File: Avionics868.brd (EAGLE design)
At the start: 86.4 x 22.9 mm, 69 parts, among them SW1 B3U-1000P-2P-SMD, U1 ATSAMD21G18_QFN, U2 SPX3819M5-L-3-0, U3 MCP73831T-2ACI/OT, U4 MPU-9250, U5 SIM868, U6 BMP280, X1 JSTPH, X2 32.768, X3 ZX62-B-5PA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

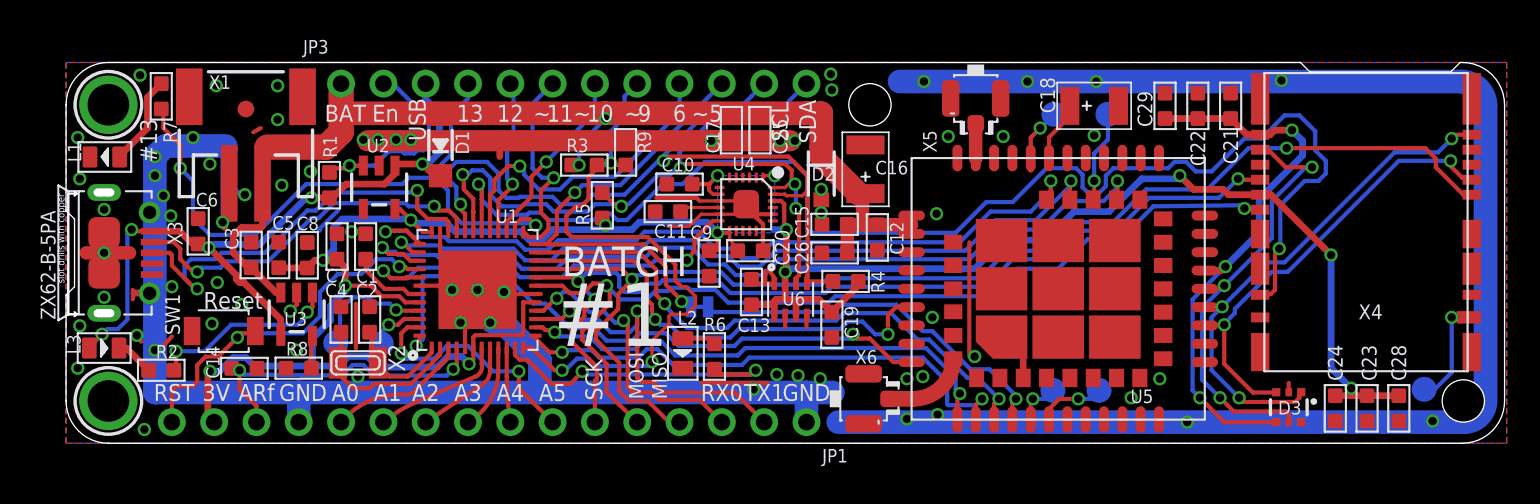
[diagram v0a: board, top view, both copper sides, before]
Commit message: Moved things around to improve capacitor placement
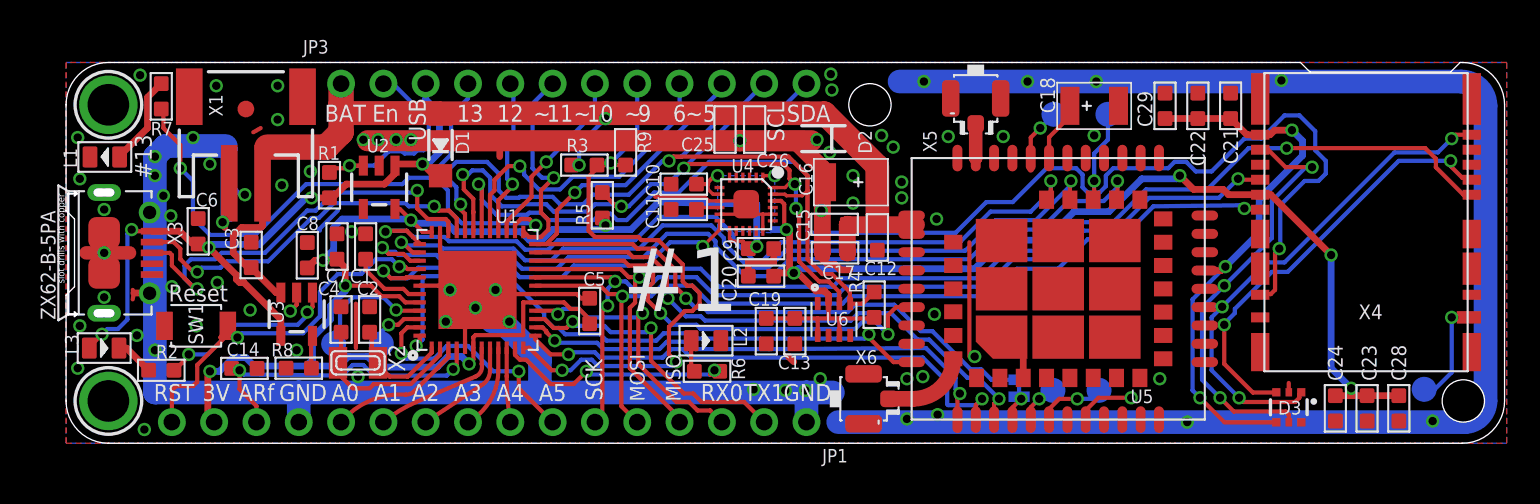
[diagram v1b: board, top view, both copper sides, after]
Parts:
- moved JP2 19.8 mm to (57.2, 3.30), turned to 270 degrees
- moved C5 19.0 mm to (31.4, 7.94)
- moved C17 9.64 mm to (46.2, 11.4), turned to 270 degrees
- moved C26 8.82 mm to (41.3, 18.8), turned to 180 degrees
- moved C19 3.96 mm to (42.0, 6.73)
- moved C13 3.51 mm to (43.8, 6.73), turned to 180 degrees
- moved C9 3.24 mm to (41.7, 11.7), turned to 270 degrees
- moved U6 2.87 mm to (46.1, 7.43)
- moved R4 2.21 mm to (48.5, 8.32), turned to 0 degrees
- moved D2 2.10 mm to (45.5, 18.3), turned to 180 degrees
- moved C25 2.10 mm to (39.6, 18.8)
- moved SW1 1.68 mm to (7.81, 7.05)
- moved C20 1.65 mm to (41.7, 10.0), turned to 90 degrees
- moved L2 1.59 mm to (38.4, 6.16), turned to 0 degrees
- moved C16 1.17 mm to (47.1, 15.7), turned to 180 degrees
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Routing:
- net D5/CTS2: track 27.0 -> 48.9 mm
- net N$6: track 22.6 -> 1.46 mm
- net GND: track 251.6 -> 262.6 mm, vias 70 -> 75
- net +3V: track 148.3 -> 157.6 mm
- net D8/GLED: track 18.7 -> 15.0 mm
- net MOSI: track 57.9 -> 55.1 mm
- net D1/TX0: track 20.6 -> 18.0 mm
- net MISO: track 74.4 -> 72.2 mm
- net SCL: track 47.8 -> 50.0 mm
- net SCK: track 58.3 -> 56.4 mm
- net SDA: track 46.9 -> 48.7 mm
- net N$23: track 3.16 -> 1.43 mm
- net VBAT: track 71.5 -> 73.0 mm
- net TX5/GPS_RX: track 47.5 -> 48.5 mm
- net RX5/GPS_TX: track 46.6 -> 47.5 mm
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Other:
- board text removed: "BATCH"

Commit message: Added some more connections to improve ground covg
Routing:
- net GND: vias 75 -> 98

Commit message: Switched Tantanum AVX-B caps with Ceramic C1206
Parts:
- C16, C18: device Seeed-Capacitor-2016:AVX-B -> Seeed-Capacitor-2016:C1206
- moved C16 0.27 mm to (46.9, 15.5)
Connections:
- net GND: now also C16.2, C18.2; no longer C16.-, C18.-
- net N$29: now also C18.1; no longer C18.+
- net VBAT: now also C16.1; no longer C16.+
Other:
- board text added: "GPS"
- board text added: "GSM"
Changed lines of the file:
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@@
 <layer number="25" name="tNames" color="7" fill="1" visible="yes" active="yes"/>
 <layer number="26" name="bNames" color="7" fill="1" visible="yes" active="yes"/>
-<layer number="27" name="tValues" color="7" fill="1" visible="yes" active="yes"/>
-<layer number="28" name="bValues" color="7" fill="1" visible="yes" active="yes"/>
+<layer number="27" name="tValues" color="7" fill="1" visible="no" active="yes"/>
+<layer number="28" name="bValues" color="7" fill="1" visible="no" active="yes"/>
 <layer number="29" name="tStop" color="7" fill="3" visible="yes" active="yes"/>
 <layer number="30" name="bStop" color="7" fill="6" visible="yes" active="yes"/>
@@
 <wire x1="74.676" y1="22.2885" x2="83.1215" y2="22.2885" width="0" layer="20"/>
 <wire x1="83.1215" y1="22.2885" x2="83.693" y2="22.86" width="0" layer="20"/>
+<text x="51.8795" y="20.7645" size="1.016" layer="21" ratio="12" rot="R270" align="center">GSM</text>
+<text x="48.006" y="5.2705" size="1.016" layer="21" ratio="12" rot="R180" align="center">GPS</text>
 </plain>
 <attributes>
@@
 <attribute name="VALUE" x="40.2971" y="12.7635" size="0.8128" layer="27" font="vector" ratio="18"/>
 </element>
-<element name="C16" library="Seeed-Capacitor-2016" package="AVX-B" value="100uf" x="47.117" y="15.6718" smashed="yes" rot="R180">
-<attribute name="MPN" value="TAJB107M010#NJ" x="47.117" y="26.3398" size="1.778" layer="27" rot="R180" display="off"/>
-<attribute name="NAME" x="44.0055" y="16.8402" size="0.8128" layer="25" ratio="18" rot="R270"/>
-<attribute name="VALUE" x="47.879" y="14.4018" size="0.8128" layer="27" ratio="18" rot="R90"/>
-<attribute name="NAME" x="47.6885" y="15.4178" size="0.4064" layer="33" ratio="18" rot="R180"/>
+<element name="C16" library="Seeed-Capacitor-2016" package="C1206" value="100uf" x="46.9265" y="15.4813" smashed="yes" rot="R180">
+<attribute name="MPN" value="GRM31CR60J107ME39L" x="46.9265" y="26.1493" size="1.778" layer="27" rot="R180" display="off"/>
+<attribute name="NAME" x="43.561" y="16.4592" size="0.8128" layer="25" ratio="18" rot="R270"/>
+<attribute name="VALUE" x="47.6885" y="14.2113" size="0.8128" layer="27" ratio="18" rot="R90"/>
+<attribute name="NAME" x="47.498" y="15.2273" size="0.4064" layer="33" ratio="18" rot="R180"/>
 </element>
 <element name="C17" library="Seeed-Capacitor-2016" package="C0603" value="10uf" x="46.1645" y="11.43" smashed="yes" rot="R270">
@@
 </element>
 <element name="X6" library="Seeed-Connector -2016" package="U-FL3P-SMD-2.6X2.6X1.0MM" value="U-FL" x="47.879" y="2.667" smashed="yes" rot="R180">
-<attribute name="NAME" x="48.7045" y="5.588" size="0.8128" layer="25" ratio="18" rot="R180"/>
+<attribute name="NAME" x="45.593" y="5.2705" size="0.8128" layer="25" ratio="18" rot="R270"/>
 </element>
 <element name="X5" library="Seeed-Connector -2016" package="U-FL3P-SMD-2.6X2.6X1.0MM" value="U-FL" x="54.61" y="20.701" smashed="yes" rot="R90">
-<attribute name="NAME" x="52.2605" y="17.4625" size="0.8128" layer="25" ratio="18" rot="R90"/>
+<attribute name="NAME" x="57.531" y="19.685" size="0.8128" layer="25" ratio="18" rot="R90"/>
 </element>
 <element name="TP4" library="microbuilder" package="TESTPOINT_ROUND_1.5MM" value="" x="62.5475" y="19.7485" smashed="yes" rot="MR0">
@@
 <attribute name="VALUE" x="78.0415" y="17.2215" size="0.889" layer="27" font="vector" ratio="18" rot="R180" align="center"/>
 </element>
-<element name="C18" library="Seeed-Capacitor-2016" package="AVX-B" value="100uf" x="61.722" y="20.2565" smashed="yes">
-<attribute name="MPN" value="TAJB107M010#NJ" x="61.722" y="20.2565" size="1.778" layer="27" display="off"/>
-<attribute name="NAME" x="59.3725" y="19.812" size="0.889" layer="25" ratio="11" rot="R90"/>
+<element name="C18" library="Seeed-Capacitor-2016" package="C1206" value="100uf" x="61.722" y="20.2565" smashed="yes">
+<attribute name="MPN" value="GRM31CR60J107ME39L" x="61.722" y="20.2565" size="1.778" layer="27" display="off"/>
+<attribute name="NAME" x="59.182" y="19.177" size="0.889" layer="25" ratio="11" rot="R90"/>
 <attribute name="VALUE" x="59.817" y="18.0975" size="0.635" layer="27" ratio="10"/>
 <attribute name="NAME" x="61.087" y="20.2565" size="0.4064" layer="33" ratio="10"/>
@@
 <wire x1="28.448" y1="5.0165" x2="28.448" y2="3.048" width="1.4224" layer="16"/>
 <wire x1="17.399" y1="5.715" x2="17.399" y2="8.382" width="0.254" layer="1"/>
-<contactref element="C18" pad="-"/>
+<contactref element="C18" pad="2"/>
 <contactref element="R9" pad="2"/>
 <via x="25.781" y="9.2075" extent="1-16" drill="0.5"/>
@@
 <contactref element="X5" pad="GND1"/>
 <contactref element="X5" pad="GND2"/>
-<contactref element="C16" pad="-"/>
+<contactref element="C16" pad="2"/>
 <contactref element="C17" pad="2"/>
 <contactref element="D2" pad="A"/>
@@
 <wire x1="30.7975" y1="17.907" x2="32.385" y2="19.4945" width="0.254" layer="16"/>
 <via x="32.385" y="19.4945" extent="1-16" drill="0.5"/>
-<contactref element="C16" pad="+"/>
+<contactref element="C16" pad="1"/>
 <contactref element="C17" pad="1"/>
 <contactref element="C12" pad="1"/>
@@
 <wire x1="22.479" y1="19.757" x2="22.479" y2="20.32" width="0.4064" layer="1"/>
 <wire x1="22.479" y1="20.32" x2="16.51" y2="20.32" width="0.4064" layer="1"/>
-<wire x1="48.7045" y1="16.637" x2="48.5775" y2="15.6718" width="0" layer="19" extent="1-1"/>
+<wire x1="48.7045" y1="16.637" x2="48.5775" y2="15.4813" width="0" layer="19" extent="1-1"/>
 <wire x1="48.7045" y1="13.1191" x2="48.7045" y2="13.335" width="0" layer="19" extent="1-1"/>
 <wire x1="50.763" y1="13.671" x2="51.054" y2="13.1191" width="0" layer="19" extent="1-1"/>
@@
 <signal name="N$29">
 <contactref element="U5" pad="28_"/>
-<contactref element="C18" pad="+"/>
+<contactref element="C18" pad="1"/>
 <wire x1="59.013" y1="17.121" x2="59.013" y2="18.373" width="0.254" layer="1"/>
 <wire x1="59.013" y1="18.373" x2="60.2615" y2="19.6215" width="0.254" layer="1"/>
-<wire x1="60.2615" y1="19.6215" x2="60.2615" y2="20.2565" width="0.254" layer="1"/>
+<wire x1="60.2615" y1="19.6215" x2="60.071" y2="20.2565" width="0.254" layer="1"/>
 </signal>
 <signal name="GPS_ANT">

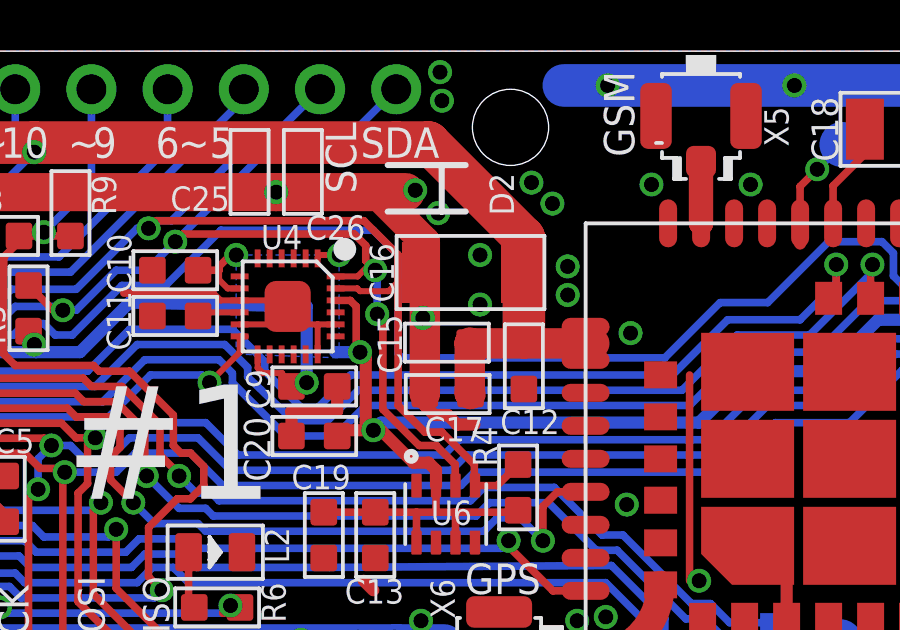
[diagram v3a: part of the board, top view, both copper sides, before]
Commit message: fixed a short circuit introduced when changing the 100uF caps to ceramic
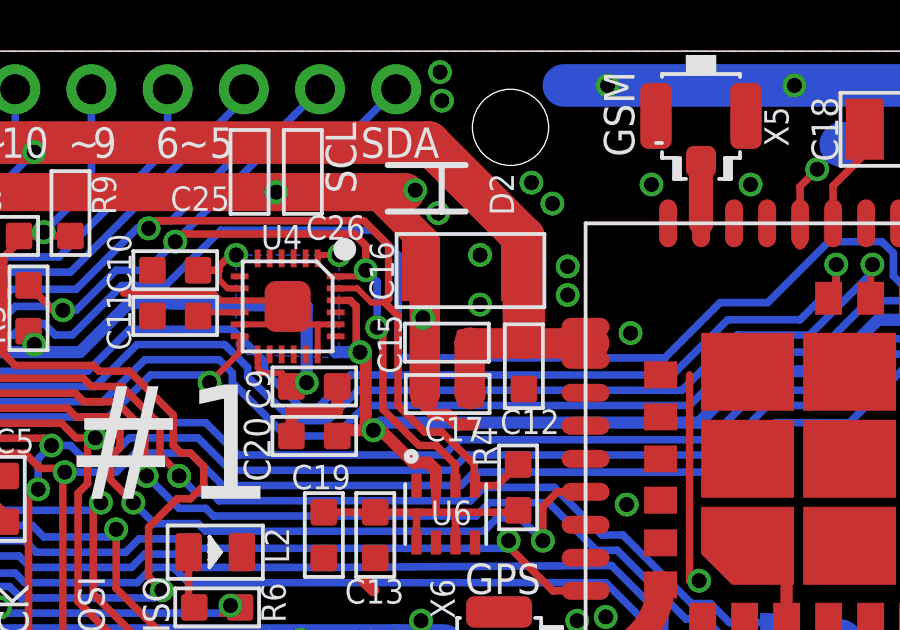
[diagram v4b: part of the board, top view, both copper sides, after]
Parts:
- moved C16 0.06 mm to (46.9, 15.5)
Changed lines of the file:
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@@
 <attribute name="VALUE" x="40.2971" y="12.7635" size="0.8128" layer="27" font="vector" ratio="18"/>
 </element>
-<element name="C16" library="Seeed-Capacitor-2016" package="C1206" value="100uf" x="46.9265" y="15.4813" smashed="yes" rot="R180">
-<attribute name="MPN" value="GRM31CR60J107ME39L" x="46.9265" y="26.1493" size="1.778" layer="27" rot="R180" display="off"/>
-<attribute name="NAME" x="43.561" y="16.4592" size="0.8128" layer="25" ratio="18" rot="R270"/>
-<attribute name="VALUE" x="47.6885" y="14.2113" size="0.8128" layer="27" ratio="18" rot="R90"/>
-<attribute name="NAME" x="47.498" y="15.2273" size="0.4064" layer="33" ratio="18" rot="R180"/>
+<element name="C16" library="Seeed-Capacitor-2016" package="C1206" value="100uf" x="46.9265" y="15.5448" smashed="yes" rot="R180">
+<attribute name="MPN" value="GRM31CR60J107ME39L" x="46.9265" y="26.2128" size="1.778" layer="27" rot="R180" display="off"/>
+<attribute name="NAME" x="43.561" y="16.5227" size="0.8128" layer="25" ratio="18" rot="R270"/>
+<attribute name="VALUE" x="47.6885" y="14.2748" size="0.8128" layer="27" ratio="18" rot="R90"/>
+<attribute name="NAME" x="47.498" y="15.2908" size="0.4064" layer="33" ratio="18" rot="R180"/>
 </element>
 <element name="C17" library="Seeed-Capacitor-2016" package="C0603" value="10uf" x="46.1645" y="11.43" smashed="yes" rot="R270">
@@
 <wire x1="22.479" y1="19.757" x2="22.479" y2="20.32" width="0.4064" layer="1"/>
 <wire x1="22.479" y1="20.32" x2="16.51" y2="20.32" width="0.4064" layer="1"/>
-<wire x1="48.7045" y1="16.637" x2="48.5775" y2="15.4813" width="0" layer="19" extent="1-1"/>
+<wire x1="48.7045" y1="16.637" x2="48.5775" y2="15.5448" width="0" layer="19" extent="1-1"/>
 <wire x1="48.7045" y1="13.1191" x2="48.7045" y2="13.335" width="0" layer="19" extent="1-1"/>
 <wire x1="50.763" y1="13.671" x2="51.054" y2="13.1191" width="0" layer="19" extent="1-1"/>
@@
 <wire x1="35.814" y1="16.9545" x2="36.195" y2="16.9545" width="0.254" layer="16"/>
 <wire x1="42.4305" y1="14.951" x2="43.1515" y2="14.951" width="0.2032" layer="1"/>
-<wire x1="44.5135" y1="15.1765" x2="44.5135" y2="16.0655" width="0.254" layer="1"/>
-<wire x1="44.5135" y1="16.0655" x2="43.3705" y2="17.2085" width="0.254" layer="1"/>
 <wire x1="43.3705" y1="17.2085" x2="36.449" y2="17.2085" width="0.254" layer="1"/>
 <wire x1="36.449" y1="17.2085" x2="36.195" y2="16.9545" width="0.254" layer="1"/>
-<wire x1="43.1515" y1="14.951" x2="43.2435" y2="14.859" width="0.2032" layer="1"/>
-<wire x1="43.2435" y1="14.859" x2="44.196" y2="14.859" width="0.2032" layer="1"/>
-<wire x1="44.196" y1="14.859" x2="44.5135" y2="15.1765" width="0.2032" layer="1"/>
+<wire x1="43.1515" y1="14.951" x2="43.6245" y2="14.478" width="0.2032" layer="1"/>
+<wire x1="43.6245" y1="14.478" x2="44.069" y2="14.478" width="0.2032" layer="1"/>
+<wire x1="44.069" y1="14.478" x2="44.5135" y2="14.0335" width="0.254" layer="1"/>
 <wire x1="35.814" y1="16.9545" x2="33.782" y2="14.9225" width="0.254" layer="16"/>
 <wire x1="33.782" y1="14.9225" x2="31.623" y2="14.9225" width="0.254" layer="16"/>
@@
 <wire x1="47.076" y1="8.3795" x2="47.818" y2="8.3795" width="0.254" layer="1"/>
 <wire x1="47.818" y1="8.3795" x2="48.514" y2="9.0805" width="0.254" layer="1"/>
-<wire x1="44.5135" y1="15.1765" x2="44.5135" y2="11.049" width="0.254" layer="1"/>
+<wire x1="44.5135" y1="14.0335" x2="44.5135" y2="11.049" width="0.254" layer="1"/>
 <wire x1="44.5135" y1="11.049" x2="45.4025" y2="10.16" width="0.254" layer="1"/>
 <wire x1="45.4025" y1="10.16" x2="45.974" y2="10.16" width="0.254" layer="1"/>
@@
 <wire x1="40.0685" y1="20.32" x2="40.64" y2="20.32" width="0.254" layer="16"/>
 <wire x1="40.64" y1="20.32" x2="41.91" y2="21.59" width="0.254" layer="16"/>
+<wire x1="43.3705" y1="17.2085" x2="44.196" y2="16.383" width="0.254" layer="1"/>
+<wire x1="44.196" y1="16.383" x2="44.196" y2="14.605" width="0.254" layer="1"/>
+<wire x1="44.196" y1="14.605" x2="44.069" y2="14.478" width="0.254" layer="1"/>
 </signal>
 <signal name="SDA">
@@
 <wire x1="37.338" y1="16.764" x2="37.084" y2="16.51" width="0.254" layer="1"/>
 <via x="37.084" y="16.51" extent="1-16" drill="0.5"/>
-<via x="43.7515" y="15.5575" extent="1-16" drill="0.5"/>
-<wire x1="43.7515" y1="15.5575" x2="43.561" y2="15.748" width="0.254" layer="1"/>
-<via x="43.815" y="14.097" extent="1-16" drill="0.5"/>
-<wire x1="43.815" y1="14.097" x2="43.815" y2="15.494" width="0.254" layer="16"/>
-<wire x1="43.815" y1="15.494" x2="43.7515" y2="15.5575" width="0.254" layer="16"/>
+<via x="43.434" y="15.5575" extent="1-16" drill="0.5"/>
+<wire x1="43.434" y1="15.5575" x2="43.561" y2="15.748" width="0.254" layer="1"/>
+<via x="43.815" y="13.6525" extent="1-16" drill="0.5"/>
+<wire x1="43.815" y1="13.6525" x2="43.815" y2="15.1765" width="0.254" layer="16"/>
+<wire x1="43.815" y1="15.1765" x2="43.434" y2="15.5575" width="0.254" layer="16"/>
 <via x="33.3375" y="14.224" extent="1-16" drill="0.5"/>
 <wire x1="29.2735" y1="13.9065" x2="31.3055" y2="13.9065" width="0.254" layer="16"/>
@@
 <wire x1="33.02" y1="14.224" x2="32.1945" y2="15.0495" width="0.254" layer="1"/>
 <wire x1="33.2105" y1="14.351" x2="33.3375" y2="14.224" width="0.254" layer="16"/>
-<wire x1="44.0055" y1="10.922" x2="44.0055" y2="13.9065" width="0.254" layer="1"/>
-<wire x1="44.0055" y1="13.9065" x2="43.815" y2="14.097" width="0.254" layer="1"/>
+<wire x1="44.0055" y1="10.922" x2="44.0055" y2="13.462" width="0.254" layer="1"/>
+<wire x1="44.0055" y1="13.462" x2="43.815" y2="13.6525" width="0.254" layer="1"/>
 <wire x1="45.7835" y1="9.7155" x2="46.4185" y2="9.0805" width="0.254" layer="1"/>
 <wire x1="46.4185" y1="9.0805" x2="46.4185" y2="8.514" width="0.254" layer="1"/>
@@
 <wire x1="35.1155" y1="15.5575" x2="33.782" y2="14.224" width="0.254" layer="16"/>
 <wire x1="33.782" y1="14.224" x2="33.3375" y2="14.224" width="0.254" layer="16"/>
-<wire x1="43.434" y1="16.383" x2="43.434" y2="15.875" width="0.254" layer="1"/>
-<wire x1="43.434" y1="15.875" x2="43.7515" y2="15.5575" width="0.254" layer="1"/>
+<wire x1="43.434" y1="16.383" x2="43.434" y2="15.5575" width="0.254" layer="1"/>
 </signal>
 <signal name="D9/VOLT">

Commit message: Minor adjustments
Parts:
- moved TP3 1.27 mm to (80.3, 3.24)
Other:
- board text added: "#2"
- board text removed: "#1"
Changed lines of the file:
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@@
 <text x="43.688" y="9.7155" size="7.62" layer="22" font="vector" ratio="15" rot="MR180" align="center">HOLY SHIT</text>
 <text x="33.3375" y="20.0025" size="1.016" layer="22" ratio="12" rot="MR90" align="center">~</text>
-<text x="36.8935" y="9.8425" size="3.81" layer="21" font="vector" ratio="15" rot="R180" align="center">#1</text>
+<text x="36.8935" y="9.8425" size="3.81" layer="21" font="vector" ratio="15" rot="R180" align="center">#2</text>
 <hole x="83.8835" y="2.54" drill="2.54"/>
 <rectangle x1="78.1558" y1="-1.1557" x2="78.5368" y2="-0.7747" layer="39"/>
@@
 <attribute name="MPN" value="RC0603FR-07100KL" x="33.5915" y="17.4625" size="1.778" layer="27" rot="R180" display="off"/>
 </element>
-<element name="TP3" library="microbuilder" package="TESTPOINT_ROUND_1.5MM" value="" x="81.534" y="3.2385" smashed="yes" rot="MR180">
-<attribute name="NAME" x="80.518" y="1.9685" size="0.8128" layer="26" ratio="18" rot="MR180"/>
-<attribute name="VALUE" x="82.677" y="3.8735" size="0.4064" layer="28" ratio="10" rot="MR180"/>
+<element name="TP3" library="microbuilder" package="TESTPOINT_ROUND_1.5MM" value="" x="80.264" y="3.2385" smashed="yes" rot="MR180">
+<attribute name="NAME" x="79.248" y="1.9685" size="0.8128" layer="26" ratio="18" rot="MR180"/>
+<attribute name="VALUE" x="81.407" y="3.8735" size="0.4064" layer="28" ratio="10" rot="MR180"/>
 </element>
 <element name="C20" library="Seeed-Capacitor-2016" package="C0603" value="10uf" x="41.7195" y="10.033" smashed="yes" rot="R90">
@@
 <wire x1="84.2165" y1="7.5565" x2="83.185" y2="7.5565" width="0.254" layer="1"/>
 <via x="83.185" y="7.5565" extent="1-16" drill="0.5"/>
-<wire x1="83.185" y1="7.5565" x2="83.185" y2="4.2545" width="0.254" layer="16"/>
-<wire x1="83.185" y1="4.2545" x2="82.169" y2="3.2385" width="0.254" layer="16"/>
-<wire x1="82.169" y1="3.2385" x2="81.534" y2="3.2385" width="0.254" layer="16"/>
+<wire x1="83.185" y1="7.5565" x2="83.185" y2="6.1595" width="0.254" layer="16"/>
+<wire x1="83.185" y1="6.1595" x2="80.264" y2="3.2385" width="0.254" layer="16"/>
 </signal>
 <signal name="N$1">
